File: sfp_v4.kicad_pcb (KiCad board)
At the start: 2 copper layers, 100 x 100 mm, 332 parts, among them J101 CONN_COAXIAL, J102 CONN_COAXIAL, J103 CONN_COAXIAL, J104 CONN_COAXIAL, J105 CONN_COAXIAL, J106 CONN_COAXIAL, J201 CONN_01X03, J202 HEATSINK, J203 HEATSINK, J204 HEATSINK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

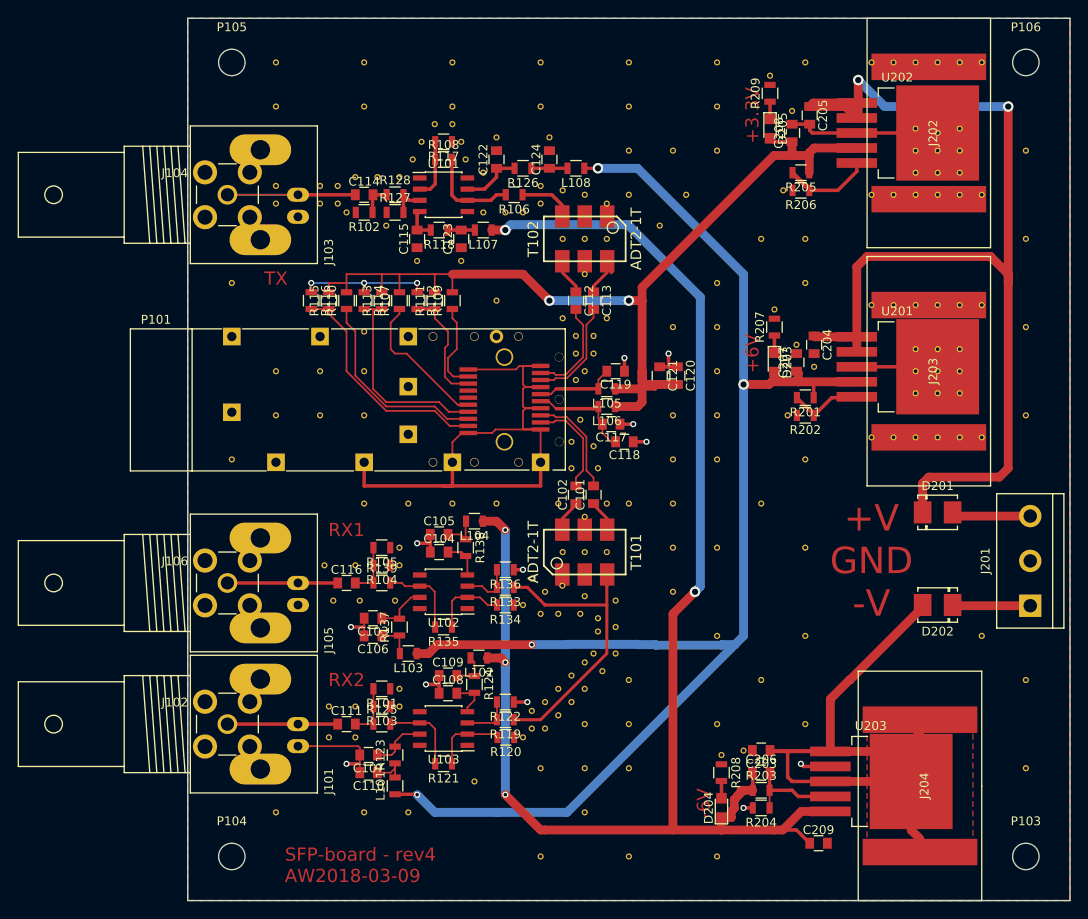
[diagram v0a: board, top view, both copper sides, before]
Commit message: revise: kicad standard lib symbols/footprints, add SFP status LEDs
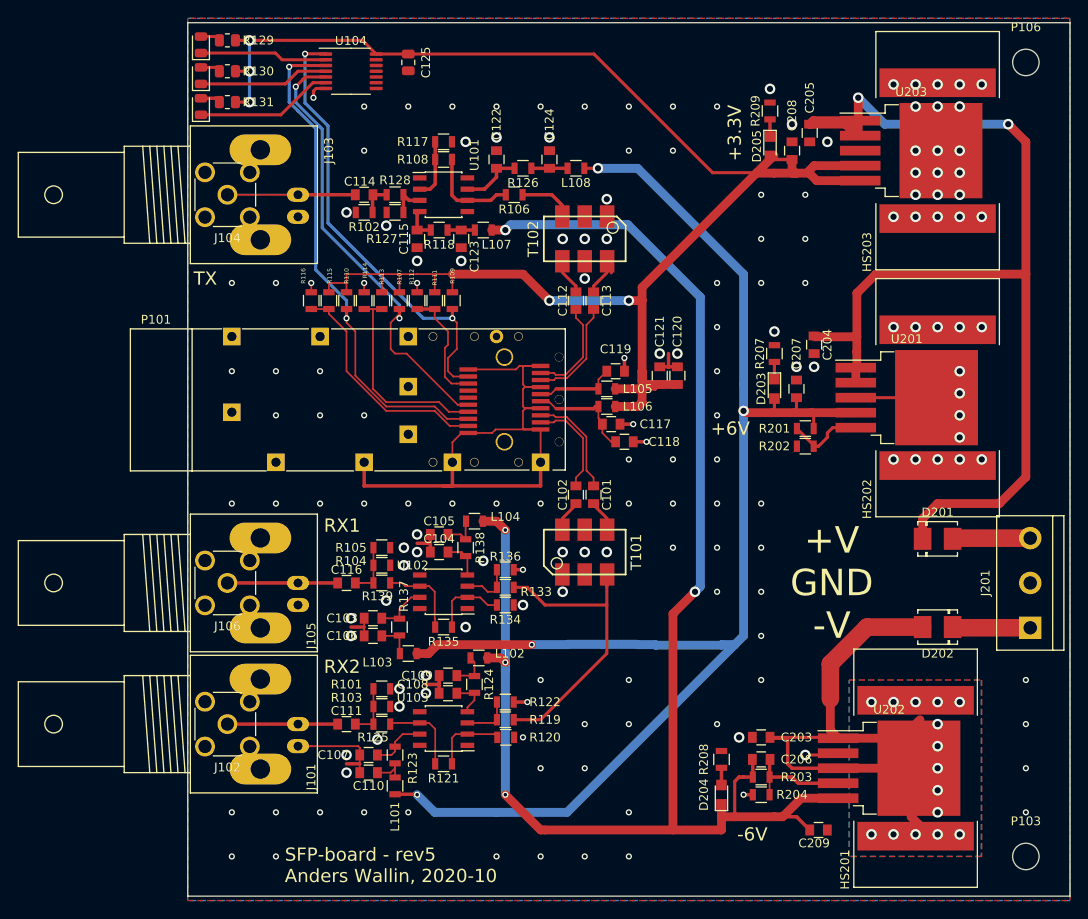
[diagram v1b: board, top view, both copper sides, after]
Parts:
- removed J202, J203, J204: HEATSINK, awallinKiCadFootprints_git:Heatsink_Fisher_TO263
- removed P104, P105: CONN_01X01, Mounting_Holes:MountingHole_3mm
- removed R205: 470R, Resistors_SMD:R_0805
- removed R206: 270R, Resistors_SMD:R_0805
- removed VIA (x221): VIA_0.4mmDrill_0.7mmPad, awallinKiCadFootprints_git:VIA_0.4mmDrill_0.7mmPad
- added C125: 100n, Capacitor_SMD:C_0805_2012Metric, F.Cu at (85.0, 45.0)
- added D101: LED, LED_SMD:LED_0805_2012Metric, F.Cu at (61.5, 43.0)
- added D102: LED, LED_SMD:LED_0805_2012Metric, F.Cu at (61.5, 46.5)
- added D103: LED, LED_SMD:LED_0805_2012Metric, F.Cu at (61.5, 50.0)
- added HS201: Heatsink_Pad, Heatsink:Heatsink_Fischer_FK24413D2PAK_26x13mm, F.Cu at (142.5, 125.0)
- added HS202: Heatsink_Pad, Heatsink:Heatsink_Fischer_FK24413D2PAK_26x13mm, F.Cu at (145.0, 83.0)
- added HS203: Heatsink_Pad, Heatsink:Heatsink_Fischer_FK24413D2PAK_26x13mm, F.Cu at (145.0, 55.0)
- added R129: 0R, Resistor_SMD:R_0805_2012Metric, F.Cu at (64.5, 42.5)
- added R130: 0R, Resistor_SMD:R_0805_2012Metric, F.Cu at (64.5, 46.0)
- added R131: 0R, Resistor_SMD:R_0805_2012Metric, F.Cu at (64.5, 49.5)
- added U104: 74HC14, Package_SO:TSSOP-14_4.4x5mm_P0.65mm, F.Cu at (78.5, 46.0)
- C101, C102, C112, C113: value C -> 100n
- J101, J103, J105: value CONN_COAXIAL -> BNC
- J102, J104, J106: value CONN_COAXIAL -> SMA; footprint awallinKiCadFootprints:CONNECTOR_SMA_Straight -> Connector_Coaxial:SMA_Molex_73251-2200_Horizontal
- L101, L102, L103, L104, L107, L108: value L -> 2u2
- R127: value 51R -> DNI
- R128: value 51R -> 0R
- R207, R208: value 1k8 -> 180R
- R209: value 680R -> 68R
- U201: value LT1963A -> LT1963AEQ; footprint TO_SOT_Packages_SMD:TO-263-5Lead -> Package_TO_SOT_SMD:TO-263-5_TabPin3
- U202: value LT1963A -> LT3015Q; footprint TO_SOT_Packages_SMD:TO-263-5Lead -> Package_TO_SOT_SMD:TO-263-5_TabPin3
- U203: value LT3015 -> LT1963AxQ-3.3; footprint TO_SOT_Packages_SMD:TO-263-5Lead -> Package_TO_SOT_SMD:TO-263-5_TabPin3
- moved U202 72.0 mm to (139.5, 125.0)
- moved U203 71.6 mm to (142.0, 55.0)
- moved U201 3.66 mm to (141.5, 83.0)
- moved R201 3.50 mm to (130.0, 86.5)
- moved R202 3.50 mm to (130.0, 88.5)
- moved C207 3.00 mm to (129.0, 82.0)
- moved D201 3.00 mm to (145.0, 99.0)
- moved D203 3.00 mm to (126.5, 82.0)
- moved R207 3.00 mm to (126.5, 78.0)
- moved D202 2.50 mm to (145.0, 109.0)
- moved J201 2.50 mm to (155.5, 104.0)
- moved C205 2.00 mm to (130.5, 53.0)
- moved C208 2.00 mm to (128.5, 55.0)
- moved D205 2.00 mm to (126.0, 54.5)
- moved R209 2.00 mm to (126.0, 50.5)
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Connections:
- U202 pad 1: Net-(C204-Pad1) -> Net-(C203-Pad1)
- U202 pad 2: Net-(C204-Pad1) -> GND
- U202 pad 3: GND -> Net-(C203-Pad1)
- U202 pad 4: +3.3V -> Net-(C206-Pad2)
- U202 pad 5: Net-(R205-Pad2) -> -6V
- U203 pad 1: Net-(C203-Pad1) -> Net-(C204-Pad1)
- U203 pad 2: GND -> Net-(C204-Pad1)
- U203 pad 3: Net-(C203-Pad1) -> GND
- U203 pad 4: Net-(C206-Pad2) -> +3.3V
- U203 pad 5: -6V -> +3.3V
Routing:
- net +3.3V: track 127.8 -> 209.9 mm, vias 2 -> 5
- net /TX-FAULT: track 10.2 -> 51.4 mm, vias 0 -> 2
- net GND: track 162.2 -> 125.2 mm, vias 15 -> 165
- net /MOD-ABS: track 16.4 -> 52.7 mm, vias 0 -> 2
- net /RX-LOS: track 22.8 -> 58.2 mm, vias 0 -> 2
- net +6V: track 192.7 -> 176.6 mm
- net Net-(D103-Pad1): track 0.00 -> 15.6 mm
- net Net-(D102-Pad1): track 0.00 -> 14.7 mm
- net Net-(R205-Pad2): track 14.7 -> 0.00 mm
- net Net-(D101-Pad1): track 0.00 -> 14.5 mm
- net Net-(C203-Pad1): track 75.2 -> 70.4 mm, vias 0 -> 15
- net Net-(C204-Pad1): track 125.1 -> 128.3 mm
- net Net-(D103-Pad2): track 0.00 -> 2.27 mm
- net Net-(D102-Pad2): track 0.00 -> 2.27 mm
- net Net-(D101-Pad2): track 0.00 -> 2.27 mm
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- added copper zone on B.Cu, net Net-(C203-Pad1)
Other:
- board size 100 x 100 mm -> 100 x 99 mm
- net class narrow: via_dia 1.2 -> 0.7; via_drill 0.7 -> 0.4
- board text added: "MOD_ABS"
- board text added: "RX_LOS"
- board text added: "SFP-board - rev5 Anders Wallin, 2020-10"
- board text added: "TX_FAULT"
- board text added: "board width reduced to 99mm, to fit 100mm wide enclosures"
- board text removed: "SFP-board - rev4 AW2018-03-09"

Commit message: simplify
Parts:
- removed R101, R103, R104, R105, R111, R114, R116, R127: DNI, Resistors_SMD:R_0805
- removed R106, R112, R128: 0R, Resistors_SMD:R_0805
- R129, R130, R131: value 0R -> 200R
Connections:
- net /RATE-SELECT0 renamed /RS0
- net /Rate-select1 renamed /RS1
- P101 pad 3: /TX-DISABLE -> GND
- R108 pad 2: Net-(R106-Pad2) -> Net-(R108-Pad2)
- T102 pad 3: Net-(R106-Pad1) -> Net-(R108-Pad2)
- U101 pad 3: Net-(R127-Pad2) -> Net-(C114-Pad2)
- U101 pad 6: Net-(R106-Pad2) -> Net-(R108-Pad2)
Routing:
- net Net-(R108-Pad2): track 0.00 -> 17.6 mm
- net /TX-DISABLE: track 13.4 -> 0.00 mm
- net Net-(R106-Pad2): track 10.7 -> 0.00 mm
- net Net-(R106-Pad1): track 5.00 -> 0.00 mm
- net Net-(R127-Pad2): track 4.11 -> 0.00 mm
- net Net-(C114-Pad2): track 3.57 -> 7.58 mm
- net Net-(C116-Pad2): track 6.05 -> 2.05 mm
- net Net-(C111-Pad2): track 6.05 -> 2.05 mm
- net GND: track 125.2 -> 128.3 mm, vias 165 -> 162
- net +3.3V: track 209.9 -> 207.8 mm
- net /RS1: track 26.2 -> 24.2 mm
- net /RS0: track 22.9 -> 21.9 mm

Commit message: revise
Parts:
- removed HS201, HS202: Heatsink_Pad, Heatsink:Heatsink_Fischer_FK24413D2PAK_26x13mm
- removed J101, J103, J105: BNC, awallinKiCadFootprints:BNC_2PIN
- added D206: D, awallinKiCadFootprints:DIODE_DO-214BA, F.Cu at (145.0, 98.5)
- added TP201: TestPoint_2Pole, TestPoint:TestPoint_2Pads_Pitch2.54mm_Drill0.8mm, F.Cu at (127.0, 133.0)
- added TP202: TestPoint_2Pole, TestPoint:TestPoint_2Pads_Pitch2.54mm_Drill0.8mm, F.Cu at (127.0, 65.0)
- added TP203: TestPoint_2Pole, TestPoint:TestPoint_2Pads_Pitch2.54mm_Drill0.8mm, F.Cu at (127.0, 87.5)
- J201: value CONN_01X03 -> Conn_01x04; footprint awallinKiCadFootprints:CONNECTOR_01x03_200mil -> TerminalBlock:TerminalBlock_bornier-4_P5.08mm
- moved J201 9.50 mm to (155.5, 113.5)
- moved C205 5.00 mm to (130.5, 58.0)
- moved C208 5.00 mm to (128.5, 60.0)
- moved D205 5.00 mm to (126.0, 59.5)
- moved HS203 5.00 mm to (145.0, 60.0)
- moved R209 5.00 mm to (126.0, 55.5)
- moved U203 5.00 mm to (142.0, 60.0)
- moved D201 4.50 mm to (145.0, 103.5)
- moved C125 3.00 mm to (85.0, 48.0)
- moved D101 3.00 mm to (61.5, 46.0)
- moved D102 3.00 mm to (61.5, 49.5)
- moved D103 3.00 mm to (61.5, 53.0)
- moved D202 3.00 mm to (145.0, 112.0)
- moved R129 3.00 mm to (64.5, 45.5)
- moved R130 3.00 mm to (64.5, 49.0)
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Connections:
- C205 pad 1: Net-(C204-Pad1) -> Net-(C205-Pad1)
- U203 pad 1: Net-(C204-Pad1) -> Net-(C205-Pad1)
- U203 pad 2: Net-(C204-Pad1) -> Net-(C205-Pad1)
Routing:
- net Net-(C205-Pad1): track 0.00 -> 93.0 mm
- net Net-(C204-Pad1): track 128.3 -> 39.8 mm
- net Net-(C203-Pad1): track 70.4 -> 46.1 mm, vias 15 -> 20
- net +3.3V: track 207.8 -> 227.2 mm, vias 5 -> 7
- net Net-(C114-Pad1): track 28.5 -> 14.5 mm
- net +VIN_FOR_3V3: track 0.00 -> 9.01 mm
- net GND: track 128.3 -> 123.0 mm, vias 162 -> 210
- net /TX-FAULT: track 51.4 -> 47.6 mm
- net /RX-LOS: track 58.2 -> 55.2 mm
- net +6V: track 176.6 -> 179.4 mm
- net /MOD-ABS: track 52.7 -> 49.9 mm
- net -6V: track 209.9 -> 212.4 mm
- net Net-(C107-Pad1): track 6.42 -> 5.78 mm
- net -VIN: track 8.83 -> 9.42 mm
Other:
- board text added: "+5V +12V GND -12V"
- board text added: "Copyright Anders E, Wallin 2020. This source describes Open Hardware and is licensed under the CERN-OHL-P v2 You may redistribute and modify this documentation and make products using it under the terms of the CERN-OHL-P v2 (https:/cern.ch/cern-ohl). This documentation is distributed WITHOUT ANY EXPRESS OR IMPLIED WARRANTY, INCLUDING OF MERCHANTABILITY, SATISFACTORY QUALITY AND FITNESS FOR A PART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"
- board text added: "No components, enclosure slots for PCB"
- board text added: "centerline"
- board text removed: "+V GND -V"

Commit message: kicad6 version
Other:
- net class Default removed
- net class narrow removed
- net class w350 removed
- net class wide removed

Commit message: update to kicad 9
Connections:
- P103 pad : GND -> (no net)
- P106 pad : GND -> (no net)
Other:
- board text added: "Enclosure Hammond 1455L1201 (120 mm x 103 mm x 31 mm) Digikey HM894-ND Meanwell (+12V, -12V, +5V) PSU with 5-pin DIN plug model GP25A13D-R1B, Digikey 1866-1826-ND"
